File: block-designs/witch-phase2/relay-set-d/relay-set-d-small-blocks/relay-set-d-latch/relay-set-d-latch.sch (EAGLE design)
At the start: 58 parts, among them IC1 74LVC1G125DBV, IC10 741G175, IC11 74LVC1G17DBV, IC12 74LVC1G17DBV, IC17 74LVC1G14DBV, IC2 74LVC1G125DBV, IC3 74LVC1G125DBV, IC4 74LVC1G125DBV, IC5 74LVC1G125DBV, IC6 741G175, IC7 741G175, IC8 741G175, IC9 741G175, Q1 MMBT2907ALT1SMD, Q2 MMBT2907ALT1SMD

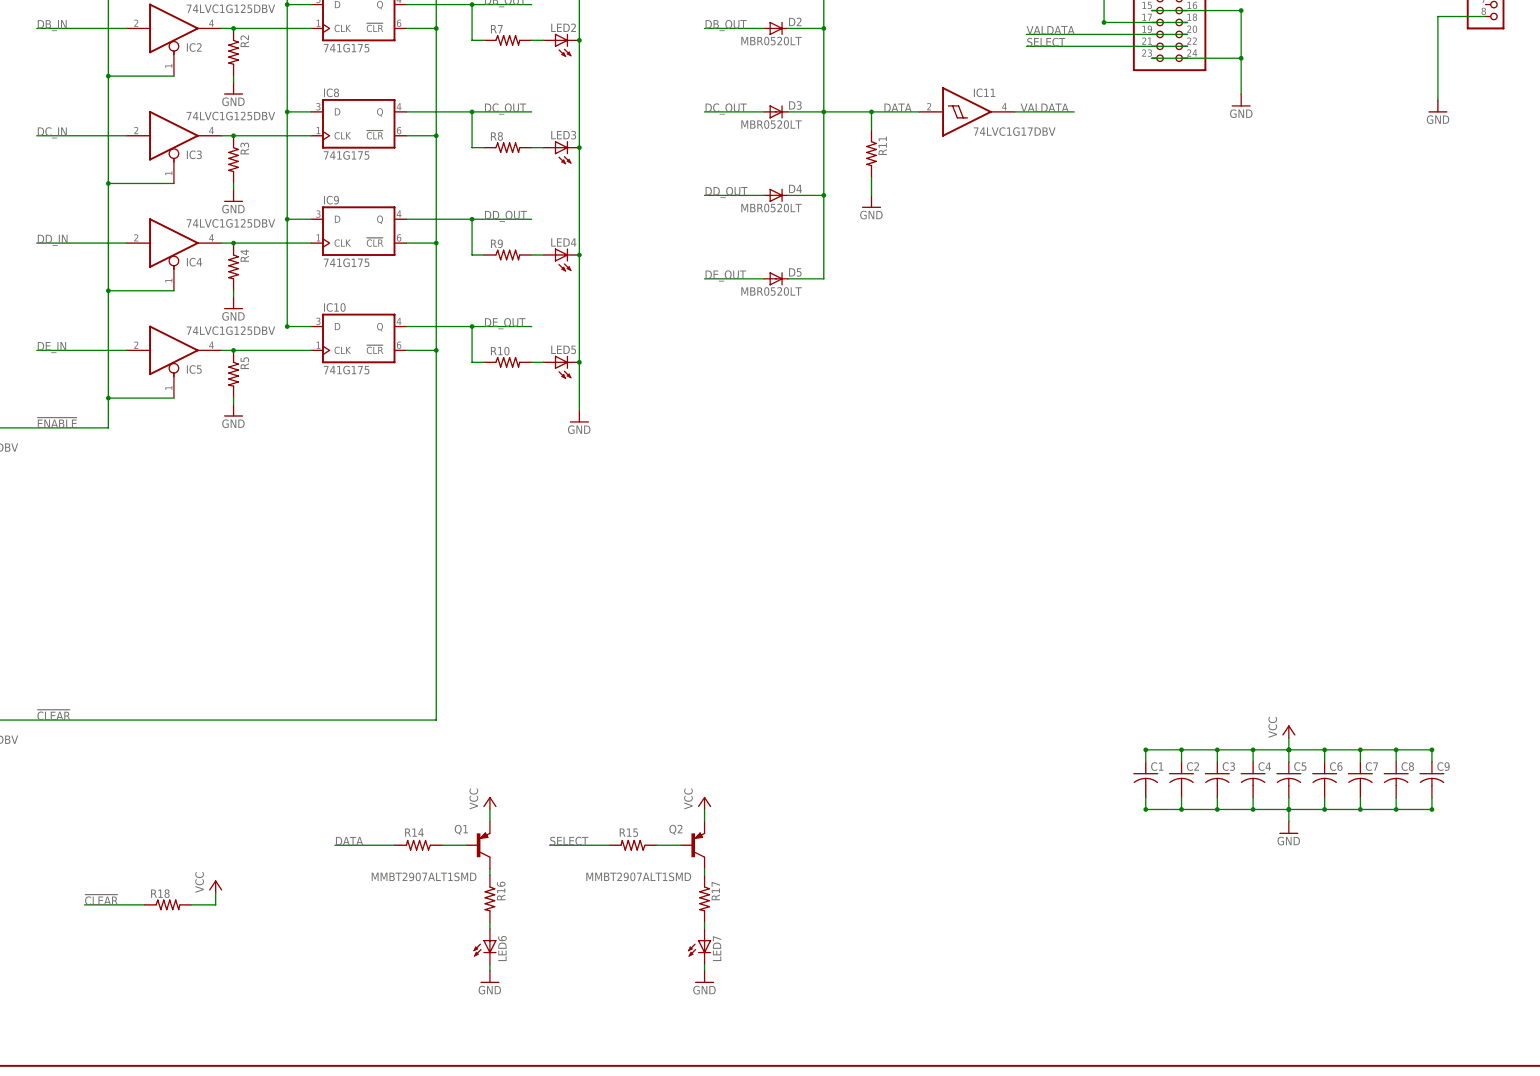
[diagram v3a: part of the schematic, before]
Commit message: rework of cabling for reset, exec, power, and key-up detection
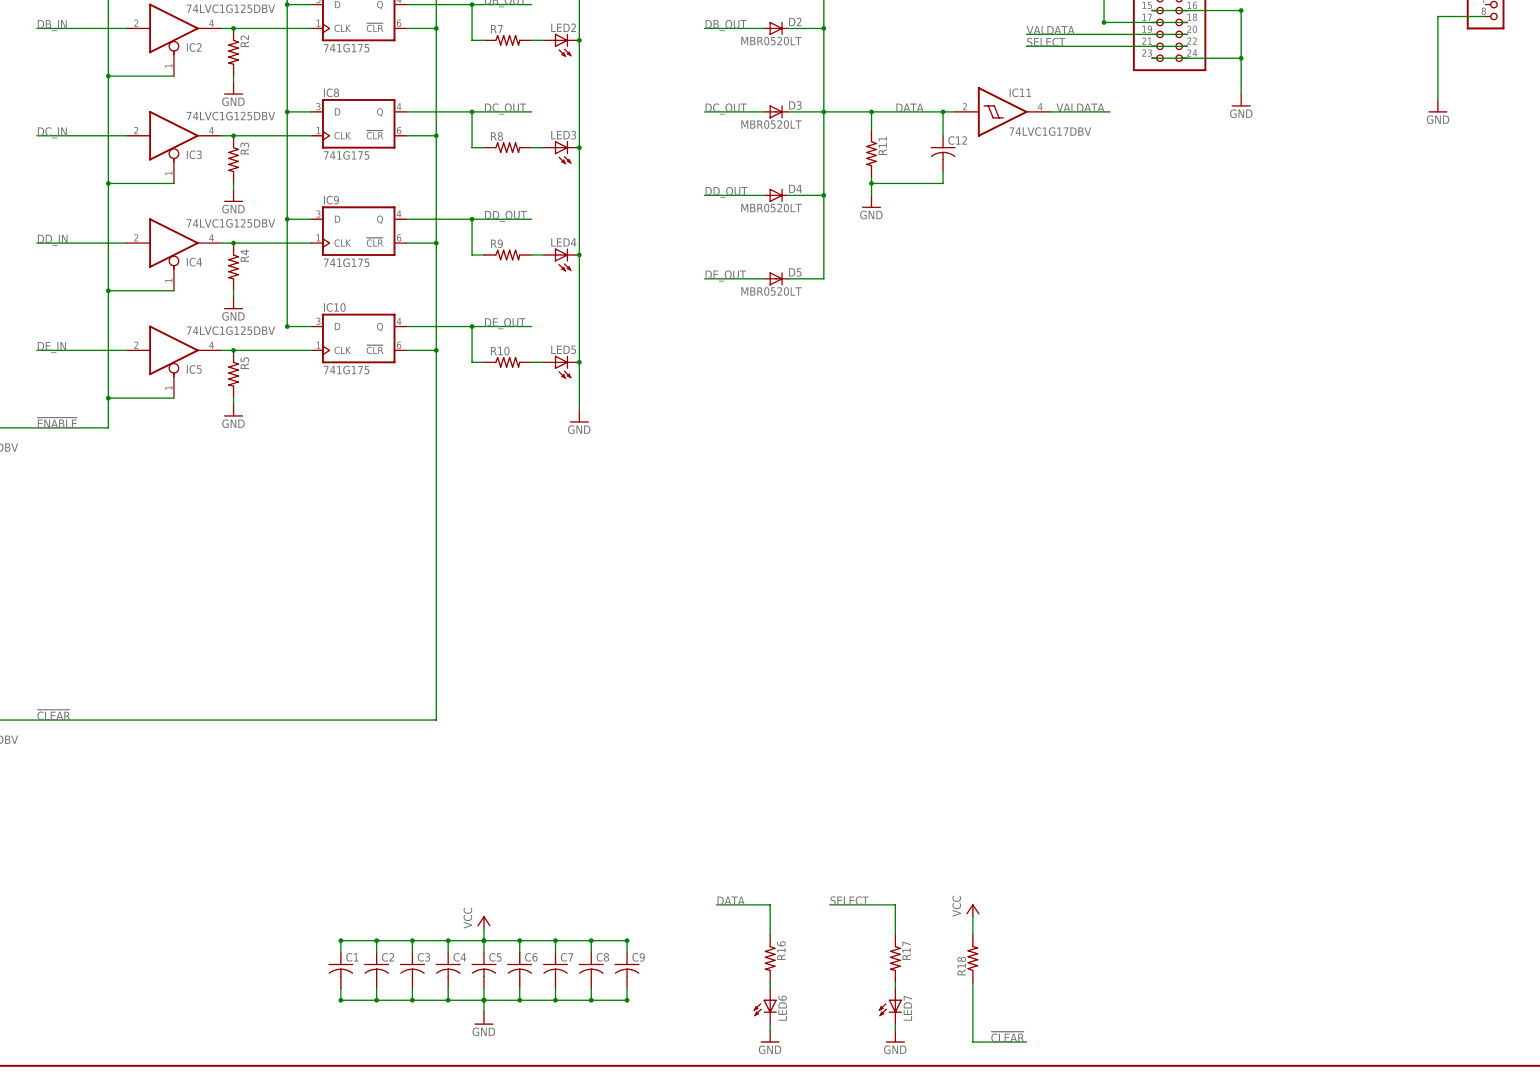
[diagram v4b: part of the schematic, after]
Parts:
- removed Q1, Q2: MMBT2907ALT1SMD, transistor-pnp:MMBT2907ALT1SMD
- removed R14, R15: (no value), resistor:R-US_R0805
- added C12: (no value), resistor:C-USC0805
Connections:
- removed net N$16: Q2.B, R15.1
- removed net N$23: Q2.C, R17.1
- removed net N$25: Q1.B, R14.1
- removed net N$26: Q1.C, R16.1
- net DATA: now also C12.1, R16.1; no longer R14.2
- net GND: now also C12.2
- net SELECT: now also R17.1; no longer R15.2
- net VCC: no longer Q1.E, Q2.E
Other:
- moved on the sheet: C1, C2, C3, C4, C5, C6, C7, C8, C9, IC11, LED6, LED7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
